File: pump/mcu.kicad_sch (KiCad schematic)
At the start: 7 parts, among them U5 AVR64DA48-I/PT

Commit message: -:
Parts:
- removed C5: 100n, symbol Device:C
- removed C6: 10n, symbol Device:C
- added R9: 330, Resistor_SMD:R_0402_1005Metric, symbol Device:R
- added SW1: SW_DPST_x2, symbol Switch:SW_DPST_x2
- C1, C3: footprint (none) -> Capacitor_SMD:C_0402_1005Metric; LCSC (none) -> C307331
- C2, C4: value 10n -> 100n; footprint (none) -> Capacitor_SMD:C_0402_1005Metric; LCSC (none) -> C307331
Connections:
- net GND: now also SW1.1 (A)
- net VDD: no longer C2.1
- net ~{RESET}: now reaches U5.40 (~{RESET}/PF6)
- net ~{RESET}: now also C2.1, R9.2
- new net: R9.1, SW1.2 (B)

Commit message: finished control relays schematic and footprints
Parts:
- SW1: footprint (none) -> Button_Switch_THT:SW_Tactile_SKHH_Angled
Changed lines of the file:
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@@
 			)
 		)
-		(property "Footprint" ""
+		(property "Footprint" "Button_Switch_THT:SW_Tactile_SKHH_Angled"
 			(at 99.06 25.4 0)
 			(effects

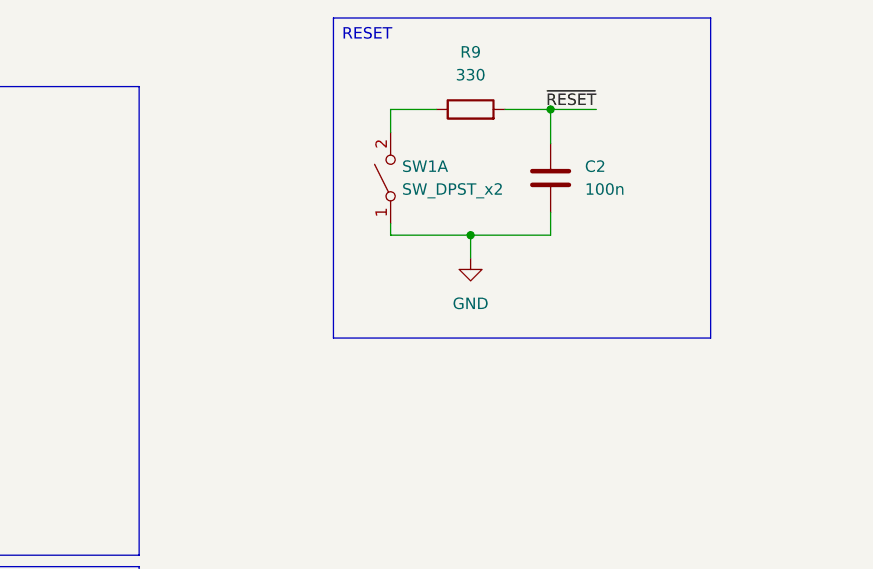
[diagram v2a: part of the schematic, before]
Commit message: finished mcu decoupling and reset cirquit
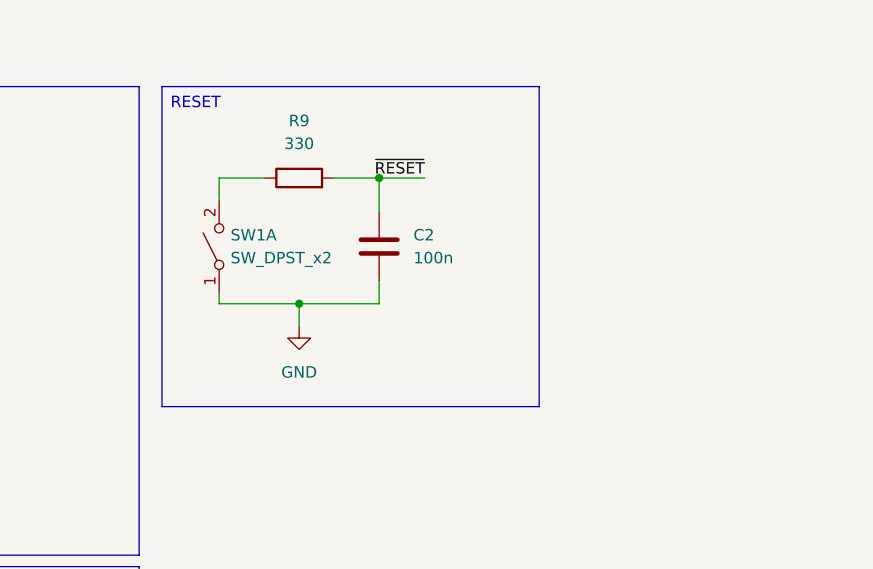
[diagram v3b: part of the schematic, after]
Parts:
- C1, C2, C3, C4: PartNo (none) -> CL05B104KB54PNC
- R9: PartNo (none) -> 0402WGF3300TCE
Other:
- moved on the sheet: C2, R9, SW1A

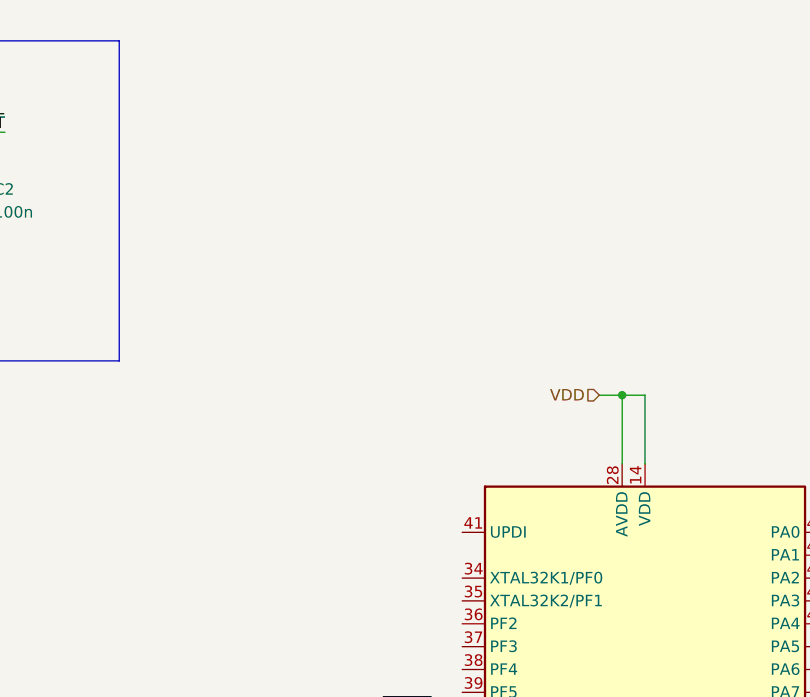
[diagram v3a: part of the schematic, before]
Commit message: added UPDI connector
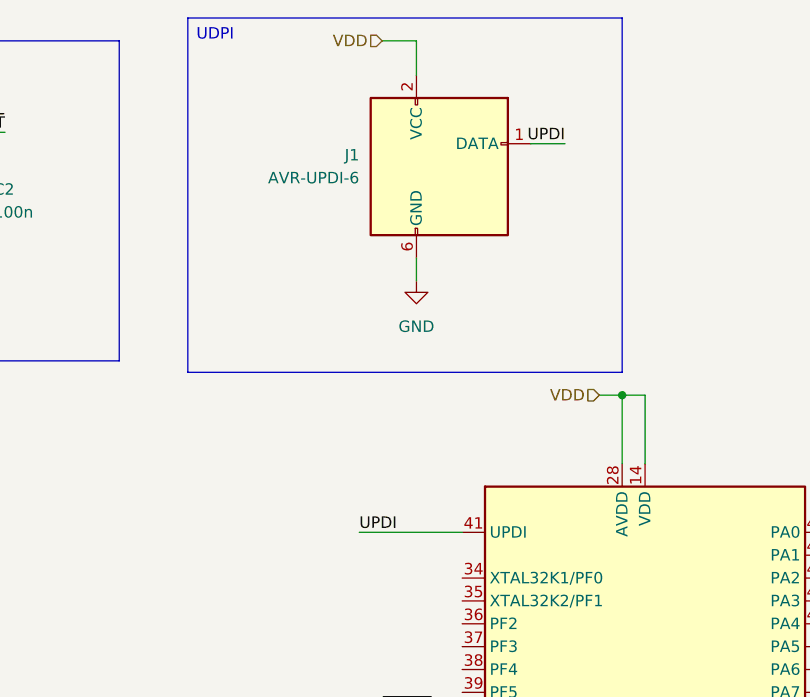
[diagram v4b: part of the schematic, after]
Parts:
- added J1: AVR-UPDI-6, Connector_PinHeader_2.54mm:PinHeader_2x03_P2.54mm_Vertical, symbol Connector:AVR-UPDI-6
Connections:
- net GND: now also J1.6 (GND)
- net VDD: now also J1.2 (VCC)
- net UPDI: now reaches U5.41 (UPDI)
- net UPDI: now also J1.1 (DATA)
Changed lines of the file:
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@@
 	(generator_version "9.0")
 	(paper "A4")
+	(text_box "UDPI"
+		(exclude_from_sim no)
+		(at 123.19 12.7 0)
+		(size 48.26 39.37)
+		(margins 0.9525 0.9525 0.9525 0.9525)
+		(stroke
+			(width 0)
+			(type solid)
+		)
+		(fill
+			(type none)
+		)
+		(effects
+			(font
+				(size 1.27 1.27)
+			)
+			(justify left top)
+		)
+	)
 	(text_box "RESET"
 		(exclude_from_sim no)
@@
 	(wire
 		(pts
+			(xy 148.59 39.37) (xy 148.59 41.91)
+		)
+		(stroke
+			(width 0)
+			(type default)
+		)
+	)
+	(wire
+		(pts
 			(xy 33.02 33.02) (xy 33.02 36.83)
 		)
@@
 	(wire
 		(pts
+			(xy 142.24 69.85) (xy 153.67 69.85)
+		)
+		(stroke
+			(width 0)
+			(type default)
+		)
+	)
+	(wire
+		(pts
 			(xy 171.45 54.61) (xy 171.45 62.23)
 		)
@@
 	(wire
 		(pts
+			(xy 161.29 26.67) (xy 165.1 26.67)
+		)
+		(stroke
+			(width 0)
+			(type default)
+		)
+	)
+	(wire
+		(pts
 			(xy 33.02 48.26) (xy 33.02 45.72)
 		)
@@
 	(wire
 		(pts
+			(xy 148.59 15.24) (xy 148.59 19.05)
+		)
+		(stroke
+			(width 0)
+			(type default)
+		)
+	)
+	(wire
+		(pts
 			(xy 173.99 54.61) (xy 173.99 62.23)
 		)
@@
 		(pts
 			(xy 144.78 90.17) (xy 153.67 90.17)
+		)
+		(stroke
+			(width 0)
+			(type default)
+		)
+	)
+	(wire
+		(pts
+			(xy 144.78 15.24) (xy 148.59 15.24)
 		)
 		(stroke
@@
 	(label "~{RESET}"
 		(at 144.78 90.17 0)
+		(effects
+			(font
+				(size 1.27 1.27)
+			)
+			(justify left bottom)
+		)
+	)
+	(label "UPDI"
+		(at 165.1 26.67 180)
+		(effects
+			(font
+				(size 1.27 1.27)
+			)
+			(justify right bottom)
+		)
+	)
+	(label "UPDI"
+		(at 142.24 69.85 0)
 		(effects
 			(font
@@
 		(shape input)
 		(at 30.48 73.66 180)
+		(effects
+			(font
+				(size 1.27 1.27)
+			)
+			(justify right)
+		)
+	)
+	(hierarchical_label "VDD"
+		(shape input)
+		(at 144.78 15.24 180)
 		(effects
 			(font
@@
 	)
 	(symbol
+		(lib_id "Connector:AVR-UPDI-6")
+		(at 151.13 29.21 0)
+		(unit 1)
+		(exclude_from_sim no)
+		(in_bom yes)
+		(on_board yes)
+		(dnp no)
+		(fields_autoplaced yes)
+		(property "Reference" "J1"
+			(at 142.24 27.9399 0)
+			(effects
+				(font
+					(size 1.27 1.27)
+				)
+				(justify right)
+			)
+		)
+		(property "Value" "AVR-UPDI-6"
+			(at 142.24 30.4799 0)
+			(effects
+				(font
+					(size 1.27 1.27)
+				)
+				(justify right)
+			)
+		)
+		(property "Footprint" "Connector_PinHeader_2.54mm:PinHeader_2x03_P2.54mm_Vertical"
+			(at 144.78 30.48 90)
+			(effects
+				(font
+					(size 1.27 1.27)
+				)
+				(hide yes)
+			)
+		)
+		(property "Datasheet" "https://www.microchip.com/webdoc/GUID-9D10622A-5C16-4405-B092-1BDD437B4976/index.html?GUID-9B349315-2842-4189-B88C-49F4E1055D7F"
+			(at 118.745 43.18 0)
+			(effects
+				(font
+					(size 1.27 1.27)
+				)
+				(hide yes)
+			)
+		)
+		(property "Description" "Atmel 6-pin UPDI connector"
+			(at 151.13 29.21 0)
+			(effects
+				(font
+					(size 1.27 1.27)
+				)
+				(hide yes)
+			)
+		)
+		(pin "3"
+		)
+		(pin "2"
+		)
+		(pin "4"
+		)
+		(pin "1"
+		)
+		(pin "6"
+		)
+		(pin "5"
+		)
+		(instances
+			(project ""
+				(path "/e0be0fc6-35a9-4dbe-8638-3e88dcb86763/bebee76a-7a2e-4d3f-b9e8-49786a5ceaea"
+					(reference "J1")
+					(unit 1)
+				)
+			)
+		)
+	)
+	(symbol
 		(lib_id "Device:C")
 		(at 97.79 33.02 0)
@@
 					(unit 1)
 				)
+			)
+		)
+	)
+	(symbol
+		(lib_id "power:GND")
+		(at 148.59 41.91 0)
+		(unit 1)
+		(exclude_from_sim no)
+		(in_bom yes)
+		(on_board yes)
+		(dnp no)
+		(fields_autoplaced yes)
+		(property "Reference" "#PWR016"
+			(at 148.59 48.26 0)
+			(effects
+				(font
+					(size 1.27 1.27)
+				)
+				(hide yes)
+			)
+		)
+		(property "Value" "GND"
+			(at 148.59 46.99 0)
+			(effects
+				(font
+					(size 1.27 1.27)
+				)
+			)
+		)
+		(property "Footprint" ""
+			(at 148.59 41.91 0)
+			(effects
+				(font
+					(size 1.27 1.27)
+				)
+				(hide yes)
+			)
+		)
+		(property "Datasheet" ""
+			(at 148.59 41.91 0)
+			(effects
+				(font
+					(size 1.27 1.27)
+				)
+				(hide yes)
+			)
+		)
+		(property "Description" "Power symbol creates a global label with name \"GND\" , ground"
+			(at 148.59 41.91 0)
+			(effects
+				(font
+					(size 1.27 1.27)
+				)
+				(hide yes)
+			)
+		)
+		(pin "1"
+		)
+		(instances
+			(project ""
+				(path "/e0be0fc6-35a9-4dbe-8638-3e88dcb86763/bebee76a-7a2e-4d3f-b9e8-49786a5ceaea"
+					(reference "#PWR016")
+					(unit 1)
+				)

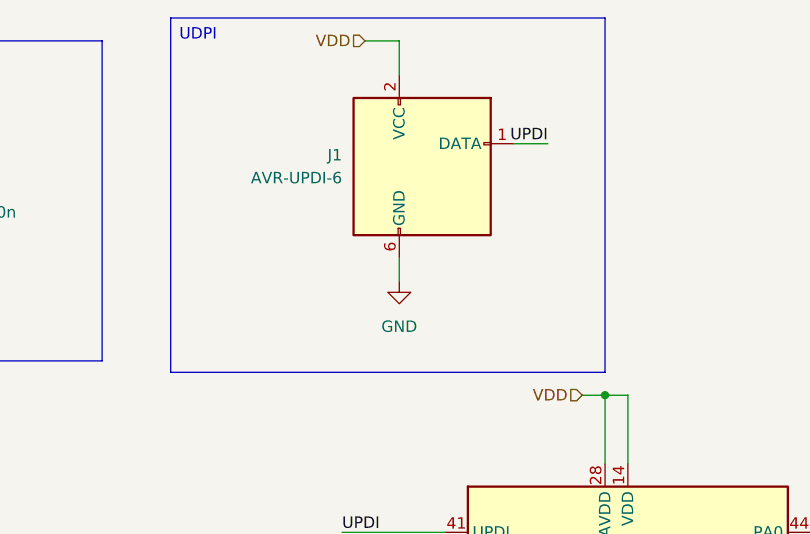
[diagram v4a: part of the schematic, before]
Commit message: added bypass cap in updi line
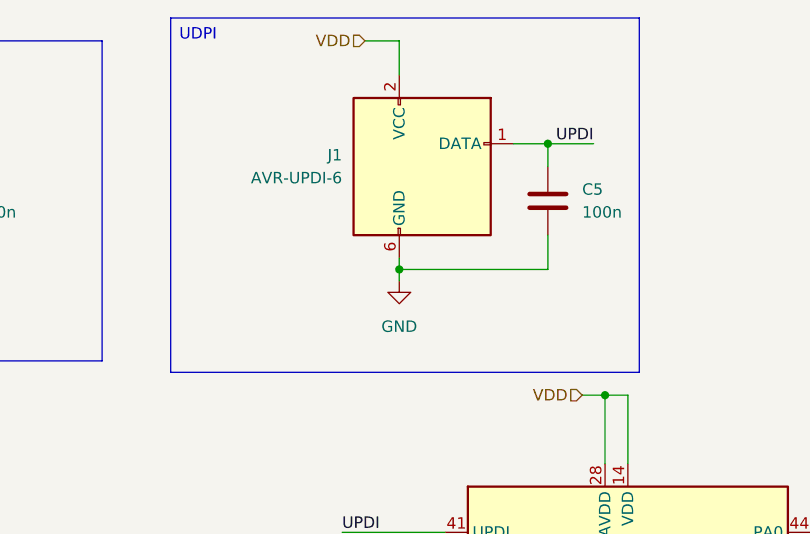
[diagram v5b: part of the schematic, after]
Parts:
- added C5: 100n, Capacitor_SMD:C_0402_1005Metric, symbol Device:C
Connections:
- net GND: now also C5.2
- net UPDI: now also C5.1
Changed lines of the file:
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@@
 		(exclude_from_sim no)
 		(at 123.19 12.7 0)
-		(size 48.26 39.37)
+		(size 52.07 39.37)
 		(margins 0.9525 0.9525 0.9525 0.9525)
 		(stroke
@@
 		(color 0 0 0 0)
 	)
+	(junction
+		(at 165.1 26.67)
+		(diameter 0)
+		(color 0 0 0 0)
+	)
+	(junction
+		(at 148.59 40.64)
+		(diameter 0)
+		(color 0 0 0 0)
+	)
 	(wire
 		(pts
@@
 	(wire
 		(pts
-			(xy 148.59 39.37) (xy 148.59 41.91)
+			(xy 165.1 40.64) (xy 148.59 40.64)
+		)
+		(stroke
+			(width 0)
+			(type default)
+		)
+	)
+	(wire
+		(pts
+			(xy 148.59 39.37) (xy 148.59 40.64)
 		)
 		(stroke
@@
 	(wire
 		(pts
+			(xy 165.1 26.67) (xy 165.1 29.21)
+		)
+		(stroke
+			(width 0)
+			(type default)
+		)
+	)
+	(wire
+		(pts
 			(xy 30.48 22.86) (xy 33.02 22.86)
 		)
@@
 	(wire
 		(pts
+			(xy 165.1 26.67) (xy 170.18 26.67)
+		)
+		(stroke
+			(width 0)
+			(type default)
+		)
+	)
+	(wire
+		(pts
 			(xy 171.45 54.61) (xy 173.99 54.61)
 		)
@@
 		(pts
 			(xy 142.24 69.85) (xy 153.67 69.85)
+		)
+		(stroke
+			(width 0)
+			(type default)
+		)
+	)
+	(wire
+		(pts
+			(xy 165.1 36.83) (xy 165.1 40.64)
+		)
+		(stroke
+			(width 0)
+			(type default)
+		)
+	)
+	(wire
+		(pts
+			(xy 148.59 40.64) (xy 148.59 41.91)
 		)
 		(stroke
@@
 	)
 	(label "UPDI"
-		(at 165.1 26.67 180)
+		(at 170.18 26.67 180)
 		(effects
 			(font
@@
 					(unit 1)
 				)
+			)
+		)
+	)
+	(symbol
+		(lib_id "Device:C")
+		(at 165.1 33.02 0)
+		(unit 1)
+		(exclude_from_sim no)
+		(in_bom yes)
+		(on_board yes)
+		(dnp no)
+		(fields_autoplaced yes)
+		(property "Reference" "C5"
+			(at 168.91 31.7499 0)
+			(effects
+				(font
+					(size 1.27 1.27)
+				)
+				(justify left)
+			)
+		)
+		(property "Value" "100n"
+			(at 168.91 34.2899 0)
+			(effects
+				(font
+					(size 1.27 1.27)
+				)
+				(justify left)
+			)
+		)
+		(property "Footprint" "Capacitor_SMD:C_0402_1005Metric"
+			(at 166.0652 36.83 0)
+			(effects
+				(font
+					(size 1.27 1.27)
+				)
+				(hide yes)
+			)
+		)
+		(property "Datasheet" "~"
+			(at 165.1 33.02 0)
+			(effects
+				(font
+					(size 1.27 1.27)
+				)
+				(hide yes)
+			)
+		)
+		(property "Description" "Unpolarized capacitor"
+			(at 165.1 33.02 0)
+			(effects
+				(font
+					(size 1.27 1.27)
+				)
+				(hide yes)
+			)
+		)
+		(property "LCSC" "C307331"
+			(at 165.1 33.02 0)
+			(effects
+				(font
+					(size 1.27 1.27)
+				)
+				(hide yes)
+			)
+		)
+		(property "PartNo" "CL05B104KB54PNC"
+			(at 165.1 33.02 0)
+			(effects
+				(font
+					(size 1.27 1.27)
+				)
+				(hide yes)
+			)
+		)
+		(pin "2"
+		)
+		(pin "1"
+		)
+		(instances
+			(project "pump"
+				(path "/e0be0fc6-35a9-4dbe-8638-3e88dcb86763/bebee76a-7a2e-4d3f-b9e8-49786a5ceaea"
+					(reference "C5")
+					(unit 1)
+				)

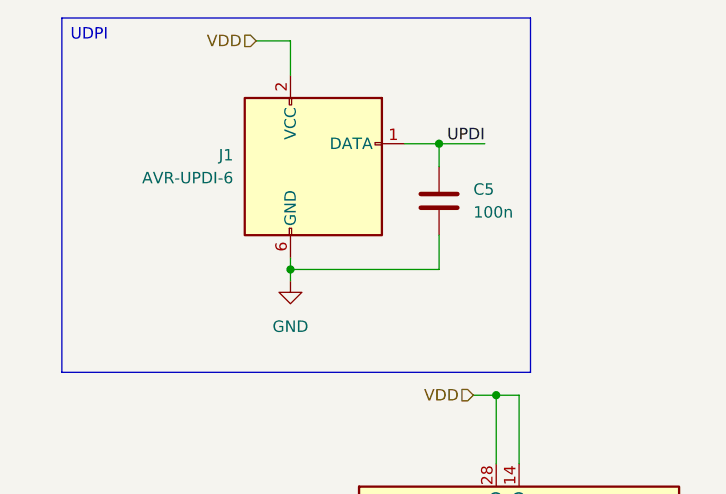
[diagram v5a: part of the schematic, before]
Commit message: Bypass on data line? LOL! Removed updi capacitor
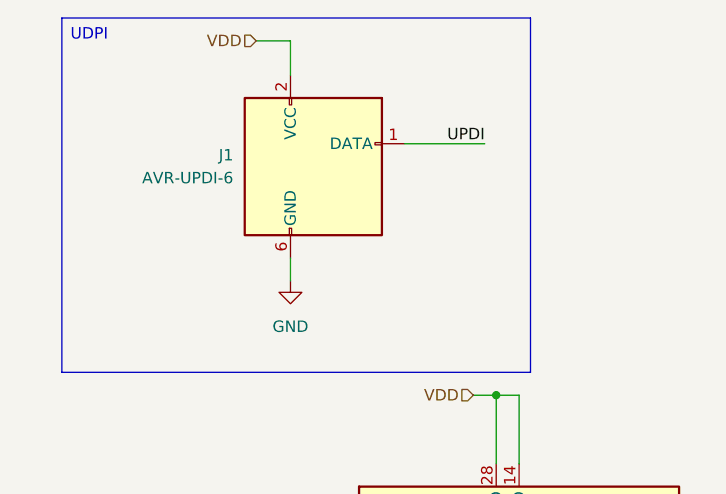
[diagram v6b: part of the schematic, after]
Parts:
- removed C5: 100n, Capacitor_SMD:C_0402_1005Metric, symbol Device:C
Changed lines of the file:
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@@
 		(color 0 0 0 0)
 	)
-	(junction
-		(at 165.1 26.67)
-		(diameter 0)
-		(color 0 0 0 0)
-	)
-	(junction
-		(at 148.59 40.64)
-		(diameter 0)
-		(color 0 0 0 0)
-	)
 	(wire
 		(pts
@@
 	(wire
 		(pts
-			(xy 165.1 40.64) (xy 148.59 40.64)
-		)
-		(stroke
-			(width 0)
-			(type default)
-		)
-	)
-	(wire
-		(pts
-			(xy 148.59 39.37) (xy 148.59 40.64)
-		)
-		(stroke
-			(width 0)
-			(type default)
-		)
-	)
-	(wire
-		(pts
 			(xy 33.02 33.02) (xy 33.02 36.83)
 		)
@@
 	(wire
 		(pts
-			(xy 165.1 26.67) (xy 165.1 29.21)
-		)
-		(stroke
-			(width 0)
-			(type default)
-		)
-	)
-	(wire
-		(pts
 			(xy 30.48 22.86) (xy 33.02 22.86)
 		)
@@
 	(wire
 		(pts
-			(xy 165.1 26.67) (xy 170.18 26.67)
+			(xy 161.29 26.67) (xy 170.18 26.67)
 		)
 		(stroke
@@
 	(wire
 		(pts
-			(xy 165.1 36.83) (xy 165.1 40.64)
-		)
-		(stroke
-			(width 0)
-			(type default)
-		)
-	)
-	(wire
-		(pts
-			(xy 148.59 40.64) (xy 148.59 41.91)
+			(xy 148.59 39.37) (xy 148.59 41.91)
 		)
 		(stroke
@@
 		(pts
 			(xy 171.45 54.61) (xy 171.45 62.23)
-		)
-		(stroke
-			(width 0)
-			(type default)
-		)
-	)
-	(wire
-		(pts
-			(xy 161.29 26.67) (xy 165.1 26.67)
 		)
 		(stroke
@@
 					(unit 1)
 				)
-			)
-		)
-	)
-	(symbol
-		(lib_id "Device:C")
-		(at 165.1 33.02 0)
-		(unit 1)
-		(exclude_from_sim no)
-		(in_bom yes)
-		(on_board yes)
-		(dnp no)
-		(fields_autoplaced yes)
-		(property "Reference" "C5"
-			(at 168.91 31.7499 0)
-			(effects
-				(font
-					(size 1.27 1.27)
-				)
-				(justify left)
-			)
-		)
-		(property "Value" "100n"
-			(at 168.91 34.2899 0)
-			(effects
-				(font
-					(size 1.27 1.27)
-				)
-				(justify left)
-			)
-		)
-		(property "Footprint" "Capacitor_SMD:C_0402_1005Metric"
-			(at 166.0652 36.83 0)
-			(effects
-				(font
-					(size 1.27 1.27)
-				)
-				(hide yes)
-			)
-		)
-		(property "Datasheet" "~"
-			(at 165.1 33.02 0)
-			(effects
-				(font
-					(size 1.27 1.27)
-				)
-				(hide yes)
-			)
-		)
-		(property "Description" "Unpolarized capacitor"
-			(at 165.1 33.02 0)
-			(effects
-				(font
-					(size 1.27 1.27)
-				)
-				(hide yes)
-			)
-		)
-		(property "LCSC" "C307331"
-			(at 165.1 33.02 0)
-			(effects
-				(font
-					(size 1.27 1.27)
-				)
-				(hide yes)
-			)
-		)
-		(property "PartNo" "CL05B104KB54PNC"
-			(at 165.1 33.02 0)
-			(effects
-				(font
-					(size 1.27 1.27)
-				)
-				(hide yes)
-			)
-		)
-		(pin "2"
-		)
-		(pin "1"
-		)
-		(instances
-			(project "pump"
-				(path "/e0be0fc6-35a9-4dbe-8638-3e88dcb86763/bebee76a-7a2e-4d3f-b9e8-49786a5ceaea"
-					(reference "C5")
-					(unit 1)
-				)
